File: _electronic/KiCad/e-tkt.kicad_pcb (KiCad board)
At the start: 2 copper layers, 71.1 x 50.8 mm, 62 parts, among them J1 USB_C_Receptacle, J2 Conn_01x04_Male, J3 Conn_01x05_Male, Q1 SS8050-G, Q2 SS8050-G, U1 ESP32-WROOM-32, U2 AMS1117-3.3, U3 CP2102N-A01-GQFN28

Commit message: pcb draft
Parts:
- removed A_driver1: Pololu_Breakout_A4988, Module:Pololu_Breakout-16_15.2x20.3mm
- removed C14, C15, C22: 0.1uF/50v(10%), Capacitor_SMD:C_0805_2012Metric
- removed C19: 0.1uF/50V(10%), Capacitor_SMD:C_0805_2012Metric
- removed C20: 4.7uF/6.3V(10%), Capacitor_SMD:C_0805_2012Metric
- removed C21: 22uF/10V(20%), Capacitor_SMD:C_0805_2012Metric
- removed D10, D9: LED, LED_SMD:LED_0805_2012Metric
- removed J2: Conn_01x04_Male, Connector_JST:JST_EH_B4B-EH-A_1x04_P2.50mm_Vertical
- removed J3: Conn_01x05_Male, Connector_JST:JST_EH_B5B-EH-A_1x05_P2.50mm_Vertical
- removed Q_hall1, Q_servo1: BSS138, Package_TO_SOT_SMD:SOT-23
- removed R21, R22: 10K(5%), Resistor_SMD:R_0805_2012Metric
- removed R23: 10K(5%)(NC), Resistor_SMD:R_0805_2012Metric
- removed R24: 2K(5%), Resistor_SMD:R_0805_2012Metric
- removed R25: 22.1K(5%), Resistor_SMD:R_0805_2012Metric
- removed R26: 47.5L(5%), Resistor_SMD:R_0805_2012Metric
- removed SW_1, SW_2, SW_wifireset1: SW_MEC_5E, Button_Switch_SMD:SW_MEC_5GSH9
- removed U_driver1: ULN2003, Package_SO:SOIC-16W_5.3x10.2mm_P1.27mm
- added A_DRIVER1: Pololu_Breakout_A4988, Module:Pololu_Breakout-16_15.2x20.3mm, B.Cu at (192.8, -178.3)
- added C10: 22uF/10V(20%), Capacitor_SMD:C_0805_2012Metric, F.Cu at (140.7, -201.6)
- added C11: 22uF/10V(20%), Capacitor_SMD:C_0805_2012Metric, F.Cu at (148.3, -219.0)
- added C12: 10uF, Capacitor_Tantalum_SMD:CP_EIA-1608-10_AVX-L, F.Cu at (160.0, -184.9)
- added C6: 22uF/10V(20%), Capacitor_SMD:C_0805_2012Metric, F.Cu at (150.4, -219.0)
- added C7: 0.1uF/50v(10%), Capacitor_SMD:C_0805_2012Metric, F.Cu at (152.4, -219.0)
- added C8: 10uF, Capacitor_Tantalum_SMD:CP_EIA-1608-10_AVX-L, F.Cu at (175.8, -175.3)
- added J_HALL1: Conn_01x03_Male, Connector_JST:JST_XH_B3B-XH-A_1x03_P2.50mm_Vertical, B.Cu at (155.6, -173.0)
- added J_LED_CAROUSEL1: Conn_01x02_Male, Connector_JST:JST_XH_B2B-XH-A_1x02_P2.50mm_Vertical, B.Cu at (182.7, -197.1)
- added J_LED_FINISH1: Conn_01x02_Male, Connector_JST:JST_XH_B2B-XH-A_1x02_P2.50mm_Vertical, B.Cu at (191.6, -197.1)
- added J_NEMA1: Conn_01x04_Male, Connector_JST:JST_XH_B4B-XH-A_1x04_P2.50mm_Vertical, B.Cu at (186.4, -173.0)
- added J_OLED1: Conn_01x04_Male, Connector_JST:JST_XH_B4B-XH-A_1x04_P2.50mm_Vertical, B.Cu at (187.6, -204.2)
- added J_SERVO1: Conn_01x03_Male, Connector_JST:JST_XH_B3B-XH-A_1x03_P2.50mm_Vertical, B.Cu at (143.8, -173.0)
- added J_STEPPER1: Conn_01x05_Male, Connector_JST:JST_XH_B5B-XH-A_1x05_P2.50mm_Vertical, B.Cu at (172.3, -173.0)
- added Q_HALL1: BSS138, Package_TO_SOT_SMD:SOT-23, F.Cu at (149.4, -177.9)
- added Q_SERVO1: BSS138, Package_TO_SOT_SMD:SOT-23, F.Cu at (137.7, -177.9)
- added R13: 10K, Resistor_SMD:R_0805_2012Metric, F.Cu at (134.6, -177.9)
- added R14: 2K(5%), Resistor_SMD:R_0805_2012Metric, F.Cu at (137.6, -200.7)
- added R15: 470, Resistor_SMD:R_0805_2012Metric, F.Cu at (172.2, -177.8)
- added R16: 470, Resistor_SMD:R_0805_2012Metric, F.Cu at (168.7, -177.8)
- added R17: 470, Resistor_SMD:R_0805_2012Metric, F.Cu at (165.1, -177.8)
- added R18: 470, Resistor_SMD:R_0805_2012Metric, F.Cu at (161.5, -177.8)
- added REF**: Symbol_Barrel_Polarity, Symbol:Symbol_Barrel_Polarity, F.Cu at (133.6, -186.4)
- added REF**: OSHW-Symbol_6.7x6mm_SilkScreen, Symbol:OSHW-Symbol_6.7x6mm_SilkScreen, F.Cu at (154.4, -196.6)
- added SW_ENABLE1: SW_DIP_x01, Button_Switch_SMD:SW_SPST_CK_RS282G05A3, F.Cu at (179.5, -211.9)
- added SW_REBOOT1: SW_DIP_x01, Button_Switch_SMD:SW_SPST_CK_RS282G05A3, F.Cu at (185.1, -211.9)
- added SW_WIFI_RESET1: SW_DIP_x01, Button_Switch_SMD:SW_SPST_CK_RS282G05A3, F.Cu at (190.7, -211.9)
- added U_DRIVER1: ULN2003, Package_SO:SOIC-16W_5.3x10.2mm_P1.27mm, F.Cu at (166.6, -188.0)
- C1: value 22uF/10V(20%) -> 4.7uF/6.3V(10%)
- C2: value ? -> 0.1uF/50V(10%)
- C3: value 22uF/10V(20%) -> 0.1uF/50v(10%)
- C4: value ? -> 0.1uF/50v(10%)
- C5: value 10uF -> 0.1uF/50v(10%); footprint Capacitor_Tantalum_SMD:CP_EIA-1608-10_AVX-L -> Capacitor_SMD:C_0805_2012Metric
- C9: value 0.1uF/50v(10%) -> 10uF; footprint Capacitor_SMD:C_0805_2012Metric -> Capacitor_Tantalum_SMD:CP_EIA-1608-10_AVX-L
- D1: value LED -> LESD5D5.0CT1G; footprint LED_SMD:LED_0805_2012Metric -> Diode_SMD:D_SOD-523
- D2, D3: value 1N4007 -> LESD5D5.0CT1G; footprint Diode_THT:D_DO-41_SOD81_P10.16mm_Horizontal -> Diode_SMD:D_SOD-523
- D5, D6, D7: value LESD5D5.0CT1G -> LED; footprint Diode_SMD:D_SOD-523 -> LED_SMD:LED_0805_2012Metric
- J1: footprint Connector_USB:USB_C_Receptacle_Amphenol_12401548E4-2A -> Connector_USB:USB_C_Receptacle_GCT_USB4115-03-C
- J_masterpower1: moved to B.Cu
- R1: value 10K -> 22.1K(5%)
- R10, R12: value 470 -> 10K
- R11: value 10K(5%) -> 10K
- R2: value 2K(5%) -> 47.5L(5%)
- R3: value 10K -> 2K(5%)
- R4, R5: value 10K -> 22
- R6: value 22 -> 10K(5%)(NC)
- R7: value 22 -> 10K(5%)
- R8, R9: value 470 -> 10K(5%)
- U2: value AMS1117-3.3 -> CP2102N-A01-GQFN28; footprint Package_TO_SOT_SMD:SOT-223-3_TabPin2 -> Package_DFN_QFN:QFN-28-1EP_5x5mm_P0.5mm_EP3.35x3.35mm
- U3: value CP2102N-A01-GQFN28 -> AMS1117-3.3; footprint Package_DFN_QFN:QFN-28-1EP_5x5mm_P0.5mm_EP3.35x3.35mm -> Package_TO_SOT_SMD:SOT-223-3_TabPin2
- moved C3 322.7 mm to (185.1, -218.0)
- moved D1 312.0 mm to (143.8, -217.4)
- moved U3 295.2 mm to (135.9, -206.3), turned to 90 degrees
- moved R2 292.9 mm to (140.7, -212.7), turned to -90 degrees
- moved C1 291.7 mm to (146.8, -213.9), turned to 180 degrees
- moved D5 291.6 mm to (171.2, -180.8)
- moved U2 291.4 mm to (147.3, -209.3), turned to -90 degrees
- moved Q1 287.8 mm to (181.1, -222.0), turned to 180 degrees
- moved Q2 287.0 mm to (188.6, -219.9), turned to -90 degrees
- moved D6 285.7 mm to (167.6, -180.8)
- moved D7 279.7 mm to (164.1, -180.8)
- moved R4 277.7 mm to (141.2, -221.5), turned to 90 degrees
- moved R11 277.4 mm to (146.3, -177.9), turned to 90 degrees
- moved C9 275.7 mm to (191.0, -175.3)
- moved R5 274.7 mm to (141.2, -217.4), turned to -90 degrees
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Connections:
- C1 pad 1: +12V -> GNDREF
- C1 pad 2: GNDREF -> +3.3V
- C2 pad 1: +12V -> GNDREF
- C2 pad 2: GNDREF -> +3.3V
- C3 pad 1: +3.3V -> GNDREF
- C3 pad 2: GNDREF -> IO0
- C4 pad 2: +3.3V -> EN
- C5 pad 1: Net-(U_driver1-Pad15) -> EN
- C9 pad 1: EN -> +3.3V
- D1 pad 1: GNDREF -> Net-(D1-Pad1)
- D1 pad 2: Net-(D1-Pad2) -> GNDREF
- D2 pad 1: GNDREF -> /USB_DN
- D2 pad 2: +12V -> GNDREF
- D3 pad 1: +3.3V -> /USB_DP
- D4 pad 1: Net-(U_driver1-Pad16) -> GNDREF
- D5 pad 1: /USB_DP -> Net-(D5-Pad1)
- D5 pad 2: GNDREF -> Net-(D5-Pad2)
- D6 pad 1: /USB_DN -> Net-(D6-Pad1)
- D6 pad 2: GNDREF -> Net-(D6-Pad2)
- D7 pad 1: /VBUS IN -> Net-(D7-Pad1)
- D7 pad 2: GNDREF -> Net-(D7-Pad2)
- D8 pad 1: Net-(U_driver1-Pad15) -> Net-(D8-Pad1)
- J1 pad A4: /VBUS IN -> Net-(D1-Pad1)
- J1 pad A9: /VBUS IN -> Net-(D1-Pad1)
- J1 pad B4: /VBUS IN -> Net-(D1-Pad1)
- J1 pad B9: /VBUS IN -> Net-(D1-Pad1)
- J_masterpower1 pad 1: Net-(J_masterpower1-Pad1) -> Net-(SWpowerswitch1-Pad5)
- R1 pad 1: SERVO -> Net-(D1-Pad1)
- R1 pad 2: +6V -> /VBUS OUT
- R10 pad 1: Net-(U_driver1-Pad15) -> HALL
- R10 pad 2: Net-(D9-Pad2) -> +6V
- R11 pad 1: +3.3V -> IO34
- R11 pad 2: EN -> +3.3V
- R12 pad 1: Net-(U_driver1-Pad15) -> SERVO
- R12 pad 2: Net-(D10-Pad2) -> +6V
- R2 pad 1: +12V -> GNDREF
- R2 pad 2: Net-(D1-Pad2) -> /VBUS OUT
- R3 pad 1: IO14 -> +3.3V
- R3 pad 2: +3.3V -> Net-(U2-Pad9)
- R4 pad 1: HALL -> /USB_DP
- R4 pad 2: +6V -> Net-(R4-Pad2)
- R5 pad 1: IO34 -> /USB_DN
- R5 pad 2: +3.3V -> Net-(R5-Pad2)
- R6 pad 1: /USB_DP -> GNDREF
- R6 pad 2: Net-(U3-Pad5) -> Net-(U2-Pad11)
- R7 pad 1: /USB_DN -> /DTR
- R7 pad 2: Net-(U3-Pad4) -> Net-(Q1-Pad1)
- R8 pad 1: Net-(U_driver1-Pad15) -> /RTS
- R8 pad 2: Net-(D4-Pad2) -> Net-(Q2-Pad1)
- R9 pad 1: Net-(U_driver1-Pad15) -> +3.3V
- R9 pad 2: Net-(D8-Pad2) -> EN
- SWpowerswitch1 pad 2: Net-(J_masterpower1-Pad1) -> Net-(SWpowerswitch1-Pad5)
- SWpowerswitch1 pad 4: unconnected-(SWpowerswitch1-Pad4) -> +12V
- SWpowerswitch1 pad 5: unconnected-(SWpowerswitch1-Pad5) -> Net-(SWpowerswitch1-Pad5)
- U2 pad 1: GNDREF -> /DCD
- U2 pad 2: +3.3V -> /RI
- U2 pad 3: +12V -> GNDREF
- U3 pad 1: /DCD -> GNDREF
- U3 pad 2: /RI -> +3.3V
- U3 pad 3: GNDREF -> +12V
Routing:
- net IO14: track 0.00 -> 69.0 mm
- net +3.3V: track 0.00 -> 65.7 mm, vias 0 -> 2
- net IO34: track 0.00 -> 64.3 mm
- net IO13: track 0.00 -> 46.9 mm, vias 0 -> 2
- net IO33: track 0.00 -> 45.1 mm, vias 0 -> 2
- net IO32: track 0.00 -> 43.4 mm, vias 0 -> 2
- net IO4: track 0.00 -> 39.7 mm
- net EN: track 0.00 -> 32.7 mm, vias 0 -> 2
- net IO15: track 0.00 -> 32.5 mm
- net +6V: track 0.00 -> 30.7 mm
- net IO25: track 0.00 -> 29.7 mm, vias 0 -> 2
- net IO0: track 0.00 -> 29.0 mm, vias 0 -> 2
- net +12V: track 0.00 -> 28.5 mm
- net IO16: track 0.00 -> 22.3 mm
- net IO5: track 0.00 -> 21.3 mm
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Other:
- board size 71.1 x 50.8 mm -> 69.8 x 62.2 mm
- board text added: "7-12v 35w"
- board text added: "E-TKT v1.1 ANDREI SPERIDIÃO andrei.cc — 2022"
- board text added: "PRESS ON BOOT TO RESET WI-FI"

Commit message: pcb draft with esp32-s3
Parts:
- removed C2: 0.1uF/50V(10%), Capacitor_SMD:C_0805_2012Metric
- removed C5: 0.1uF/50v(10%), Capacitor_SMD:C_0805_2012Metric
- removed D1, D3: LESD5D5.0CT1G, Diode_SMD:D_SOD-523
- removed D4: LED, LED_SMD:LED_0805_2012Metric
- removed J1: USB_C_Receptacle, Connector_USB:USB_C_Receptacle_GCT_USB4115-03-C
- removed R14: 2K(5%), Resistor_SMD:R_0805_2012Metric
- removed R5: 22, Resistor_SMD:R_0805_2012Metric
- removed R6: 10K(5%)(NC), Resistor_SMD:R_0805_2012Metric
- removed R9: 10K(5%), Resistor_SMD:R_0805_2012Metric
- removed SW_ENABLE1, SW_REBOOT1, SW_WIFI_RESET1: SW_DIP_x01, Button_Switch_SMD:SW_SPST_CK_RS282G05A3
- removed SWpowerswitch1: SW_DPDT_x2, Button_Switch_SMD:SW_DPDT_CK_JS202011JCQN
- removed U1: ESP32-WROOM-32, RF_Module:ESP32-WROOM-32
- removed U3: AMS1117-3.3, Package_TO_SOT_SMD:SOT-223-3_TabPin2
- removed U_6v1: L7806, Package_TO_SOT_SMD:TO-252-2
- added C13: 10nF, Capacitor_SMD:C_0603_1608Metric_Pad1.08x0.95mm_HandSolder, F.Cu at (141.7, -211.8)
- added C14: 47pF, Capacitor_SMD:C_0603_1608Metric_Pad1.08x0.95mm_HandSolder, F.Cu at (143.8, -211.8)
- added C15: 47pF, Capacitor_SMD:C_0603_1608Metric_Pad1.08x0.95mm_HandSolder, F.Cu at (145.8, -211.8)
- added C17: 100nF, Capacitor_SMD:C_0603_1608Metric_Pad1.08x0.95mm_HandSolder, F.Cu at (147.8, -217.0)
- added C18: 4.7uF, Capacitor_Tantalum_SMD:CP_EIA-1608-10_AVX-L_Pad1.25x1.05mm_HandSolder, F.Cu at (147.8, -219.0)
- added D_RX1: LED, LED_SMD:LED_0805_2012Metric, F.Cu at (150.8, -208.8)
- added D_TX1: LED, LED_SMD:LED_0805_2012Metric, F.Cu at (152.8, -208.8)
- added F2: 500mA, Fuse:Fuse_1210_3225Metric_Pad1.42x2.65mm_HandSolder, F.Cu at (143.3, -217.9)
- added FB1: FerriteBead, Inductor_SMD:L_0603_1608Metric_Pad1.05x0.95mm_HandSolder, F.Cu at (139.7, -217.9)
- added J2: USB4120-03-C_REVA, SnapEDA Library:GCT_USB4120-03-C_REVA, F.Cu at (135.7, -215.1)
- added R19: 27R, Resistor_SMD:R_0603_1608Metric_Pad0.98x0.95mm_HandSolder, F.Cu at (151.8, -204.7)
- added R20: 27R, Resistor_SMD:R_0603_1608Metric_Pad0.98x0.95mm_HandSolder, F.Cu at (151.8, -202.7)
- added R21: 5.1K(10%), Resistor_SMD:R_0603_1608Metric_Pad0.98x0.95mm_HandSolder, F.Cu at (147.8, -211.8)
- added R22: 5.1K(10%), Resistor_SMD:R_0603_1608Metric_Pad0.98x0.95mm_HandSolder, F.Cu at (139.7, -211.8)
- added REF**: KiCad-Logo2_5mm_SilkScreen, Symbol:KiCad-Logo2_5mm_SilkScreen, B.Cu at (164.6, -180.3)
- added S_BOOT1: TS06-667-25-BK-100-G-SMT-TR, SnapEDA Library:SW_TS06-667-25-BK-100-G-SMT-TR, F.Cu at (189.5, -217.4)
- added S_RESET1: TS06-667-25-BK-100-G-SMT-TR, SnapEDA Library:SW_TS06-667-25-BK-100-G-SMT-TR, F.Cu at (189.5, -209.3)
- added S_WIFIRESET1: TS06-667-25-BK-100-G-SMT-TR, SnapEDA Library:SW_TS06-667-25-BK-100-G-SMT-TR, F.Cu at (189.5, -201.2)
- added S_power1: JS202011JCQN, SnapEDA Library:SW_JS202011JCQN, F.Cu at (135.6, -205.3)
- added U6: ESP32-S3-WROOM-1-N8R2, SnapEDA Library:XCVR_ESP32-S3-WROOM-1-N16R2, F.Cu at (164.1, -214.4)
- added U_6v2: L7806, Package_TO_SOT_SMD:TO-263-3_TabPin2, F.Cu at (140.9, -183.9)
- A_DRIVER1: footprint Module:Pololu_Breakout-16_15.2x20.3mm -> SnapEDA Library:Pololu_Breakout-16_15.2x20.3mm
- C1: value 4.7uF/6.3V(10%) -> 0.1uF/50v(10%); footprint Capacitor_SMD:C_0805_2012Metric -> Capacitor_SMD:C_0603_1608Metric_Pad1.08x0.95mm_HandSolder
- C10: value 22uF/10V(20%) -> 10uF/10V(20%); footprint Capacitor_SMD:C_0805_2012Metric -> Capacitor_SMD:C_0603_1608Metric_Pad1.08x0.95mm_HandSolder
- C11, C3, C4, C6, C7: footprint Capacitor_SMD:C_0805_2012Metric -> Capacitor_SMD:C_0603_1608Metric_Pad1.08x0.95mm_HandSolder
- C12, C8, C9: footprint Capacitor_Tantalum_SMD:CP_EIA-1608-10_AVX-L -> Capacitor_Tantalum_SMD:CP_EIA-1608-10_AVX-L_Pad1.25x1.05mm_HandSolder
- D2: value LESD5D5.0CT1G -> LED; footprint Diode_SMD:D_SOD-523 -> LED_SMD:LED_0805_2012Metric
- D5, D6, D7, D8: footprint LED_SMD:LED_0805_2012Metric -> LED_SMD:LED_0603_1608Metric_Pad1.05x0.95mm_HandSolder
- J_HALL1, J_SERVO1: footprint Connector_JST:JST_XH_B3B-XH-A_1x03_P2.50mm_Vertical -> Connector_PinHeader_2.54mm:PinHeader_1x03_P2.54mm_Vertical
- J_LED_CAROUSEL1, J_LED_FINISH1: footprint Connector_JST:JST_XH_B2B-XH-A_1x02_P2.50mm_Vertical -> Connector_PinHeader_2.54mm:PinHeader_1x02_P2.54mm_Vertical
- J_NEMA1, J_OLED1: footprint Connector_JST:JST_XH_B4B-XH-A_1x04_P2.50mm_Vertical -> Connector_PinHeader_2.54mm:PinHeader_1x04_P2.54mm_Vertical
- J_STEPPER1: footprint Connector_JST:JST_XH_B5B-XH-A_1x05_P2.50mm_Vertical -> Connector_PinHeader_2.54mm:PinHeader_1x05_P2.54mm_Vertical
- J_masterpower1: footprint Connector_BarrelJack:BarrelJack_GCT_DCJ200-10-A_Horizontal -> SnapEDA Library:BarrelJack_GCT_DCJ200-10-A_Horizontal
- Q1, Q2: footprint digikey-footprints:SOT-23-3 -> Package_TO_SOT_SMD:SOT-23
- Q_HALL1, Q_SERVO1: footprint Package_TO_SOT_SMD:SOT-23 -> Package_TO_SOT_SMD:SOT-323_SC-70
- R1: value 22.1K(5%) -> 10K(5%); footprint Resistor_SMD:R_0805_2012Metric -> Resistor_SMD:R_0603_1608Metric
- R10, R11, R12, R13, R15, R16, R17, R18, R7, R8: footprint Resistor_SMD:R_0805_2012Metric -> Resistor_SMD:R_0603_1608Metric
- R2: value 47.5L(5%) -> 470R; footprint Resistor_SMD:R_0805_2012Metric -> Resistor_SMD:R_0603_1608Metric_Pad0.98x0.95mm_HandSolder
- R3: value 2K(5%) -> 470R; footprint Resistor_SMD:R_0805_2012Metric -> Resistor_SMD:R_0603_1608Metric_Pad0.98x0.95mm_HandSolder
- R4: value 22 -> 10K; footprint Resistor_SMD:R_0805_2012Metric -> Resistor_SMD:R_0603_1608Metric_Pad0.98x0.95mm_HandSolder
- REF**: moved to B.Cu
- U2: value CP2102N-A01-GQFN28 -> AZ1117I-3.3; footprint Package_DFN_QFN:QFN-28-1EP_5x5mm_P0.5mm_EP3.35x3.35mm -> Package_TO_SOT_SMD:SOT-223
- moved R4 46.9 mm to (182.4, -198.9), turned to 0 degrees
- moved R1 40.4 mm to (182.9, -217.4)
- moved C1 34.7 mm to (181.3, -217.4), turned to 90 degrees
- moved D2 16.8 mm to (139.7, -202.7)
- moved REF** 16.2 mm to (168.1, -188.0), turned to 180 degrees
- moved C11 14.8 mm to (138.7, -207.8)
- moved R8 11.2 mm to (180.8, -214.9)
- moved R2 11.1 mm to (151.8, -213.4), turned to 0 degrees
- moved Q2 11.0 mm to (180.9, -212.1)
- moved R7 10.6 mm to (177.3, -213.2)
- moved C3 10.4 mm to (177.3, -211.2)
- moved J_OLED1 10.3 mm to (193.3, -195.6), turned to 90 degrees
- moved R3 10.2 mm to (151.8, -211.8)
- moved REF** 7.69 mm to (134.6, -194.1), turned to -90 degrees
- moved J_masterpower1 7.66 mm to (143.3, -194.1)
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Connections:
- net IO34 renamed IO9
- A_DRIVER1 pad 15: IO32 -> IO36
- A_DRIVER1 pad 16: IO33 -> IO45
- A_DRIVER1 pad 9: IO25 -> IO35
- C1 pad 1: GNDREF -> EN
- C1 pad 2: +3.3V -> GNDREF
- C10 pad 1: +12V -> /VIN
- C11 pad 1: +3.3V -> Net-(C11-Pad1)
- D2 pad 1: /USB_DN -> Net-(C11-Pad1)
- D2 pad 2: GNDREF -> +3.3V
- J_LED_CAROUSEL1 pad 2: IO17 -> IO37
- J_LED_FINISH1 pad 2: IO5 -> IO38
- J_OLED1 pad 3: IO22 -> IO48
- J_OLED1 pad 4: IO21 -> IO47
- Q_SERVO1 pad 2: IO14 -> IO10
- R1 pad 1: Net-(D1-Pad1) -> +3.3V
- R1 pad 2: /VBUS OUT -> EN
- R13 pad 1: IO14 -> IO10
- R2 pad 1: GNDREF -> +5V
- R2 pad 2: /VBUS OUT -> Net-(D_TX1-Pad2)
- R3 pad 1: +3.3V -> +5V
- R3 pad 2: Net-(U2-Pad9) -> Net-(D_RX1-Pad2)
- R4 pad 1: /USB_DP -> +3.3V
- R4 pad 2: Net-(R4-Pad2) -> IO39
- U2 pad 1: /DCD -> GNDREF
- U2 pad 2: /RI -> +3.3V
- U2 pad 3: GNDREF -> /VIN
- U2 pad 4: Net-(R5-Pad2) -> +3.3V
- U_DRIVER1 pad 1: IO15 -> IO14
- U_DRIVER1 pad 2: IO4 -> IO13
- U_DRIVER1 pad 3: IO2 -> IO12
- U_DRIVER1 pad 4: IO16 -> IO11
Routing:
- net GNDREF: track 11.4 -> 325.4 mm, vias 0 -> 12
- net +3.3V: track 65.7 -> 205.5 mm, vias 2 -> 9
- net +12V: track 28.5 -> 91.8 mm, vias 0 -> 6
- net IO10: track 0.00 -> 54.5 mm, vias 0 -> 4
- net IO14: track 69.0 -> 15.0 mm
- net IO33: track 45.1 -> 0.00 mm, vias 2 -> 0
- net IO32: track 43.4 -> 0.00 mm, vias 2 -> 0
- net +5V: track 0.00 -> 42.5 mm
- net IO45: track 0.00 -> 40.6 mm, vias 0 -> 2
- net IO4: track 39.7 -> 0.00 mm
- net Net-(C14-Pad2): track 0.00 -> 36.1 mm, vias 0 -> 4
- net IO15: track 32.5 -> 0.00 mm
- net IO36: track 0.00 -> 32.2 mm, vias 0 -> 2
- net IO38: track 0.00 -> 31.9 mm, vias 0 -> 2
- net IO13: track 46.9 -> 15.0 mm, vias 2 -> 0
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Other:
- board size 69.8 x 62.2 mm -> 71.1 x 63 mm
- board text added: "**orientation**"
- board text added: "9-12v 35w"
- board text added: "ANDREI SPERIDIÃO andrei.cc — 2022"
- board text added: "E-TKT"
- board text added: "RESET + WIFI"
- board text added: "github.com/andreisperid/E-TKT"
- board text added: "v1.1"
- board text removed: "7-12v 35w"
- board text removed: "E-TKT v1.1 ANDREI SPERIDIÃO andrei.cc — 2022"
- board text removed: "PRESS ON BOOT TO RESET WI-FI"

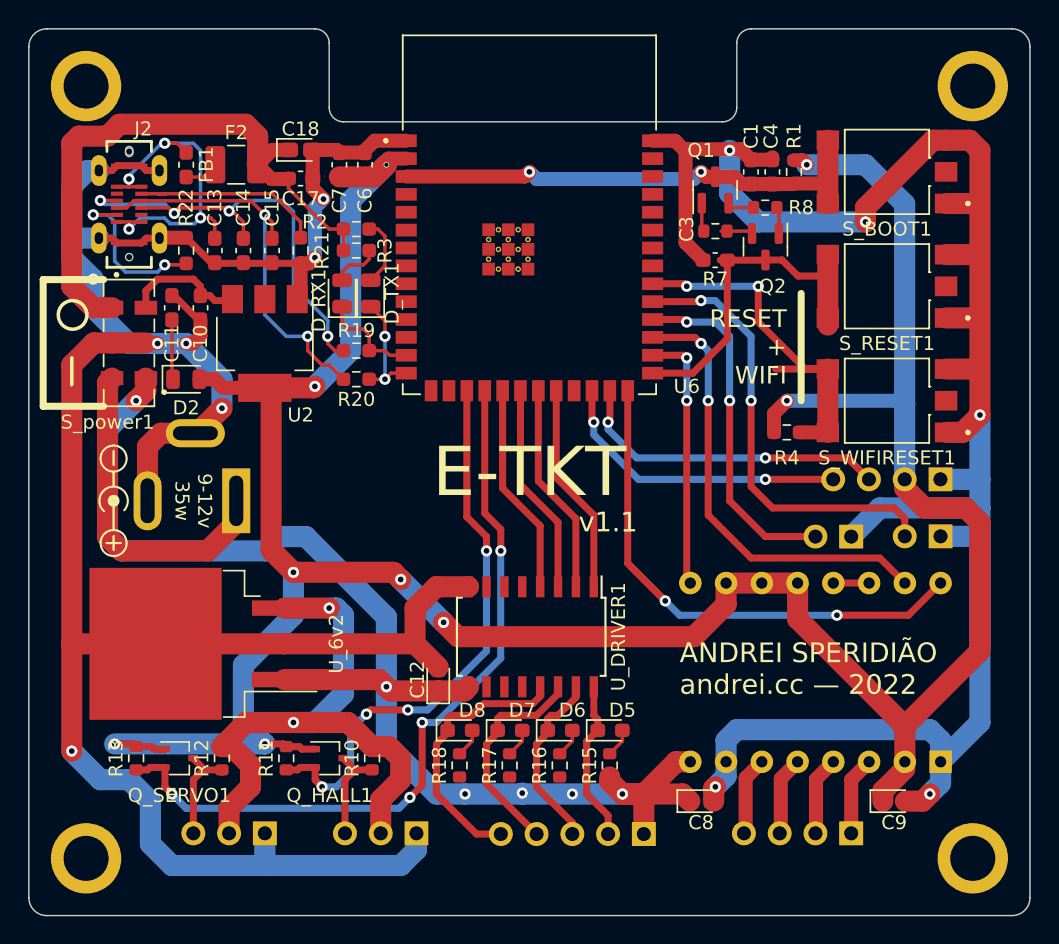
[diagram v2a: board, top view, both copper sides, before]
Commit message: improved pcb design, with parts in stock
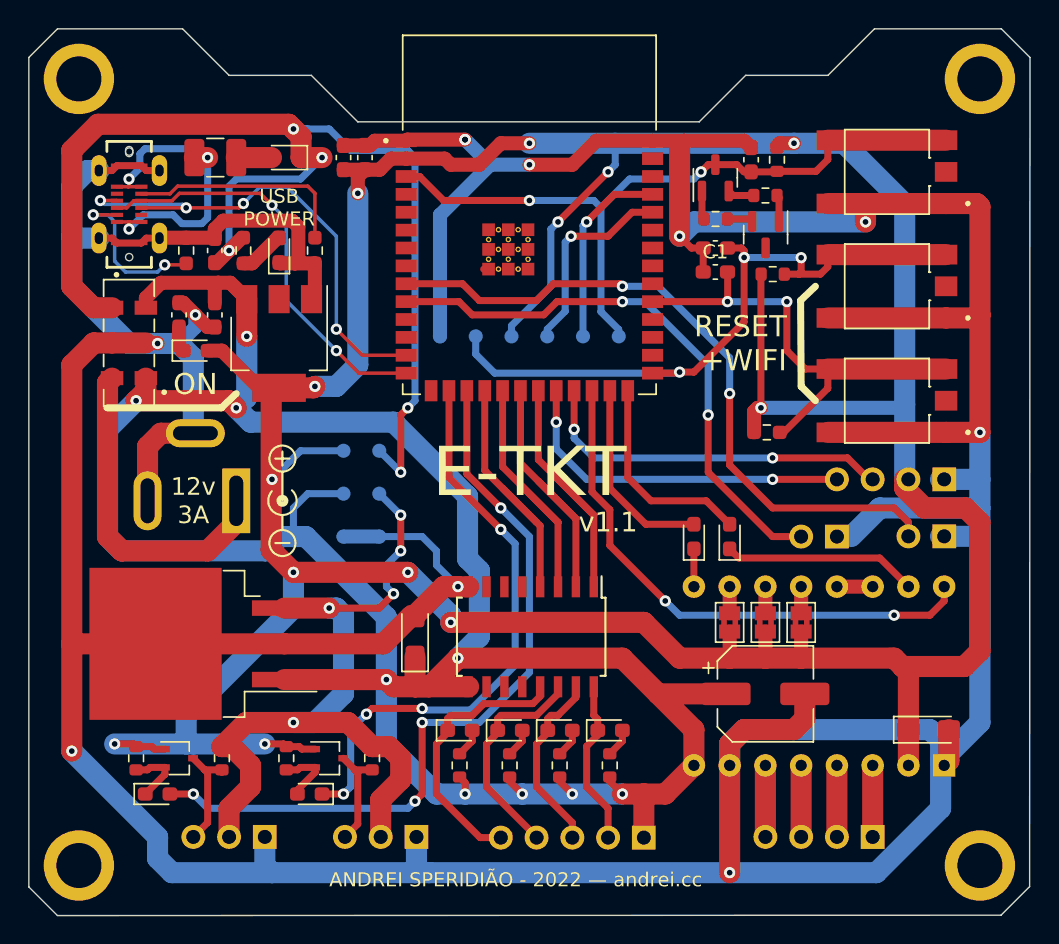
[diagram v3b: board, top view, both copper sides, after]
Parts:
- removed C14, C15: 47pF, Capacitor_SMD:C_0603_1608Metric_Pad1.08x0.95mm_HandSolder
- removed C17: 100nF, Capacitor_SMD:C_0603_1608Metric_Pad1.08x0.95mm_HandSolder
- removed C18: 4.7uF, Capacitor_Tantalum_SMD:CP_EIA-1608-10_AVX-L_Pad1.25x1.05mm_HandSolder
- removed D_RX1, D_TX1: LED, LED_SMD:LED_0805_2012Metric
- removed FB1: FerriteBead, Inductor_SMD:L_0603_1608Metric_Pad1.05x0.95mm_HandSolder
- removed R19, R20: 27R, Resistor_SMD:R_0603_1608Metric_Pad0.98x0.95mm_HandSolder
- removed R2, R3: 470R, Resistor_SMD:R_0603_1608Metric_Pad0.98x0.95mm_HandSolder
- removed the REF** at (164.6, -180.3)
- added D1: LED, LED_SMD:LED_0603_1608Metric_Pad1.05x0.95mm_HandSolder, F.Cu at (178.3, -191.5)
- added D10: LED, LED_SMD:LED_0603_1608Metric_Pad1.05x0.95mm_HandSolder, F.Cu at (137.7, -173.2)
- added D3: BAT760,115, Diode_SMD:D_SOD-323, F.Cu at (146.8, -218.4)
- added D4: LED, LED_SMD:LED_0603_1608Metric_Pad1.05x0.95mm_HandSolder, F.Cu at (175.8, -191.5)
- added D9: LED, LED_SMD:LED_0603_1608Metric_Pad1.05x0.95mm_HandSolder, F.Cu at (148.5, -173.2)
- added D_USBIN1: LED, LED_SMD:LED_0603_1608Metric_Pad1.05x0.95mm_HandSolder, F.Cu at (146.3, -211.9)
- added JP1: SolderJumper_2_Bridged, Jumper:SolderJumper-2_P1.3mm_Bridged2Bar_Pad1.0x1.5mm, F.Cu at (178.3, -185.4)
- added JP2: SolderJumper_2_Bridged, Jumper:SolderJumper-2_P1.3mm_Bridged2Bar_Pad1.0x1.5mm, F.Cu at (180.8, -185.4)
- added JP3: SolderJumper_2_Bridged, Jumper:SolderJumper-2_P1.3mm_Bridged2Bar_Pad1.0x1.5mm, F.Cu at (183.4, -185.4)
- added R5: 10K(5%), Resistor_SMD:R_0603_1608Metric, F.Cu at (181.4, -210.2)
- added R6: 100R, Resistor_SMD:R_0603_1608Metric_Pad0.98x0.95mm_HandSolder, F.Cu at (143.8, -211.8)
- added TP_12v1: TestPoint, TestPoint:TestPoint_Pad_D1.0mm, B.Cu at (150.9, -194.6)
- added TP_3.3v1: TestPoint, TestPoint:TestPoint_Pad_D1.0mm, B.Cu at (150.9, -197.6)
- added TP_5v1: TestPoint, TestPoint:TestPoint_Pad_D1.0mm, B.Cu at (153.4, -197.6)
- added TP_6v1: TestPoint, TestPoint:TestPoint_Pad_D1.0mm, B.Cu at (153.4, -194.6)
- added TP_CTS1: TestPoint, TestPoint:TestPoint_Pad_D1.0mm, B.Cu at (160.3, -205.7)
- added TP_DTR1: TestPoint, TestPoint:TestPoint_Pad_D1.0mm, B.Cu at (170.4, -205.7)
- added TP_GND1: TestPoint, TestPoint:TestPoint_Pad_D1.0mm, B.Cu at (157.7, -205.7)
- added TP_GND2: TestPoint, TestPoint:TestPoint_Pad_D1.0mm, B.Cu at (150.9, -191.5)
- added TP_GND3: TestPoint, TestPoint:TestPoint_Pad_D1.0mm, B.Cu at (153.4, -191.5)
- added TP_RX1: TestPoint, TestPoint:TestPoint_Pad_D1.0mm, B.Cu at (167.9, -205.7)
- added TP_TX1: TestPoint, TestPoint:TestPoint_Pad_D1.0mm, B.Cu at (165.3, -205.7)
- added TP_VCC_3.3V1: TestPoint, TestPoint:TestPoint_Pad_D1.0mm, B.Cu at (162.8, -205.7)
- C12, C9: footprint Capacitor_Tantalum_SMD:CP_EIA-1608-10_AVX-L_Pad1.25x1.05mm_HandSolder -> Capacitor_Tantalum_SMD:CP_EIA-3216-10_Kemet-I_Pad1.58x1.35mm_HandSolder
- C13: value 10nF -> 10uF/25v
- C8: value 10uF -> 100uF; footprint Capacitor_Tantalum_SMD:CP_EIA-1608-10_AVX-L_Pad1.25x1.05mm_HandSolder -> Capacitor_SMD:CP_Elec_6.3x5.9
- D2: footprint LED_SMD:LED_0805_2012Metric -> LED_SMD:LED_0603_1608Metric_Pad1.05x0.95mm_HandSolder
- R15, R16, R17, R18: value 470 -> 430R
- R4: value 10K -> 10K(5%)
- moved REF** 11.8 mm to (146.5, -194.1), turned to 90 degrees
- moved C8 8.89 mm to (180.8, -180.3)
- moved C1 8.19 mm to (177.3, -210.3), turned to 0 degrees
- moved C9 5.64 mm to (192.4, -177.8)
- moved REF** 5.08 mm to (164.1, -184.9)
- moved C12 3.48 mm to (156.0, -184.4)
- moved D2 2.14 mm to (140.4, -204.7)
- moved F2 1.57 mm to (141.8, -218.4)
- moved J_17HS4023_1 1.55 mm to (188.5, -170.2)
- moved R1 1.48 mm to (181.7, -218.3)
- moved R4 1.42 mm to (181.0, -198.9)
- moved C10 1.14 mm to (141.7, -207.3)
- moved J_LED_PRESS1 1.02 mm to (185.9, -191.5)
- moved R21 1.02 mm to (148.8, -211.8)
- moved U2 1.02 mm to (146.3, -205.2)
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- renumbered J_NEMA1 to J_17HS4023_1, J_STEPPER1 to J_28byj-48-12v_1, J_LED_FINISH1 to J_LED_END1, J_LED_CAROUSEL1 to J_LED_PRESS1
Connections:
- A_DRIVER1 pad 10: +3.3V -> Net-(JP1-Pad2)
- A_DRIVER1 pad 11: +3.3V -> Net-(A_DRIVER1-Pad11)
- A_DRIVER1 pad 12: +3.3V -> Net-(A_DRIVER1-Pad12)
- A_DRIVER1 pad 15: IO36 -> Net-(A_DRIVER1-Pad15)
- A_DRIVER1 pad 16: IO45 -> IO47
- A_DRIVER1 pad 9: IO35 -> Net-(A_DRIVER1-Pad9)
- C1 pad 1: EN -> GNDREF
- C1 pad 2: GNDREF -> IO38
- C10 pad 1: /VIN -> +12V
- C13 pad 2: Net-(C13-Pad2) -> +5V
- C3 pad 2: IO0 -> IO0 RESET
- F2 pad 2: +5V -> Net-(D3-Pad2)
- J2 pad A4: Net-(C13-Pad2) -> Net-(F2-Pad1)
- J2 pad A6: Net-(C15-Pad2) -> IO20 D+
- J2 pad A7: Net-(C14-Pad2) -> IO19 D-
- J2 pad A9: Net-(C13-Pad2) -> Net-(F2-Pad1)
- J2 pad B4: Net-(C13-Pad2) -> Net-(F2-Pad1)
- J2 pad B6: Net-(C15-Pad2) -> IO20 D+
- J2 pad B7: Net-(C14-Pad2) -> IO19 D-
- J2 pad B9: Net-(C13-Pad2) -> Net-(F2-Pad1)
- J_LED_END1 pad 2: IO38 -> IO16
- J_LED_PRESS1 pad 2: IO37 -> IO17
- J_OLED1 pad 3: IO48 -> IO21
- J_OLED1 pad 4: IO47 -> IO14
- Q_HALL1 pad 2: IO9 -> Net-(D9-Pad2)
- Q_SERVO1 pad 2: IO10 -> Net-(D10-Pad1)
- R1 pad 1: +3.3V -> EN
- R1 pad 2: EN -> +3.3V
- R11 pad 1: IO9 -> Net-(D9-Pad2)
- R13 pad 1: IO10 -> Net-(D10-Pad1)
- R4 pad 1: +3.3V -> IO38
- R4 pad 2: IO39 -> +3.3V
- S_BOOT1 pad 2: GNDREF -> EN
- S_BOOT1 pad 3: EN -> GNDREF
- S_RESET1 pad 2: GNDREF -> IO0 RESET
- S_RESET1 pad 3: IO0 -> GNDREF
- S_RESET1 pad 4: IO0 -> IO0 RESET
- S_WIFIRESET1 pad 2: GNDREF -> IO38
- S_WIFIRESET1 pad 3: IO39 -> GNDREF
- S_WIFIRESET1 pad 4: IO39 -> IO38
- S_power1 pad 3: /VIN -> +12V
- U2 pad 3: /VIN -> +12V
- U6 pad 11: IO18 -> unconnected-(U6-Pad11)
- U6 pad 12: IO8 -> unconnected-(U6-Pad12)
- U6 pad 13: IO19 -> IO19 D-
- U6 pad 14: IO20 -> IO20 D+
- U6 pad 15: IO3 -> unconnected-(U6-Pad15)
- U6 pad 17: IO9 -> IO09
- U6 pad 27: IO0 -> IO0 RESET
- U6 pad 28: IO35 -> unconnected-(U6-Pad28)
- U6 pad 29: IO36 -> unconnected-(U6-Pad29)
- U6 pad 30: IO37 -> unconnected-(U6-Pad30)
- U6 pad 32: IO39 -> unconnected-(U6-Pad32)
- U6 pad 33: IO40 -> unconnected-(U6-Pad33)
- U6 pad 34: IO41 -> unconnected-(U6-Pad34)
- U6 pad 35: IO42 -> unconnected-(U6-Pad35)
- U6 pad 36: unconnected-(U6-Pad36) -> RXD0
- U6 pad 37: unconnected-(U6-Pad37) -> TXD0
- U6 pad 38: IO2 -> unconnected-(U6-Pad38)
- U6 pad 39: IO1 -> unconnected-(U6-Pad39)
- U6 pad 4: IO4 -> unconnected-(U6-Pad4)
- U6 pad 5: IO5 -> unconnected-(U6-Pad5)
- U6 pad 6: IO6 -> unconnected-(U6-Pad6)
- U6 pad 7: IO7 -> unconnected-(U6-Pad7)
- U6 pad 8: IO15 -> unconnected-(U6-Pad8)
- U_DRIVER1 pad 1: IO14 -> IO13
- U_DRIVER1 pad 2: IO13 -> IO12
- U_DRIVER1 pad 3: IO12 -> IO11
- U_DRIVER1 pad 4: IO11 -> IO10
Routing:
- net +12V: track 91.8 -> 188.3 mm, vias 6 -> 9
- net GNDREF: track 325.4 -> 419.0 mm, vias 12 -> 11
- net +3.3V: track 205.5 -> 266.6 mm, vias 9 -> 13
- net IO09: track 0.00 -> 54.8 mm, vias 0 -> 4
- net IO16: track 0.00 -> 49.1 mm, vias 0 -> 2
- net IO0 RESET: track 0.00 -> 48.5 mm, vias 0 -> 3
- net +5V: track 42.5 -> 84.0 mm, vias 0 -> 5
- net IO46: track 0.00 -> 41.4 mm, vias 0 -> 4
- net IO9: track 40.2 -> 0.00 mm, vias 4 -> 0
- net IO17: track 0.00 -> 40.2 mm, vias 0 -> 2
- net Net-(C14-Pad2): track 36.1 -> 0.00 mm, vias 4 -> 0
- net IO19 D-: track 0.00 -> 36.0 mm, vias 0 -> 4
- net IO10: track 54.5 -> 19.0 mm, vias 4 -> 0
- net IO36: track 32.2 -> 0.00 mm, vias 2 -> 0
- net IO20 D+: track 0.00 -> 29.6 mm, vias 0 -> 2
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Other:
- outline, holes or cut-outs redrawn
- board text added: "12v"
- board text added: "12v 3A"
- board text added: "3.3v"
- board text added: "5v"
- board text added: "6v"
- board text added: "ANDREI SPERIDIÃO - 2022 — andrei.cc"
- board text added: "CTS"
- board text added: "DISPLAY"
- board text added: "DTR"
- board text added: "EXTERNAL FLASHING"
- board text added: "GND"
- board text added: "HALL"
- board text added: "LED END"
- board text added: "LED PRESS"
- board text added: "NEMA"
- board text added: "ON"
- board text added: "RESET +WIFI"
- board text added: "RX"
- board text added: "SERVO"
- board text added: "STEPPER"
- board text added: "TX"
- board text added: "USB POWER"
- board text added: "VCC 3.3v"
- board text added: "VMOT"
- board text removed: "**orientation**"
- board text removed: "9-12v 35w"
- board text removed: "ANDREI SPERIDIÃO andrei.cc — 2022"
- board text removed: "RESET + WIFI"
